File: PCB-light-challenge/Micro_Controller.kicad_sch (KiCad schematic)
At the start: 11 parts, among them J1 Conn_01x16_Socket, J3 Conn_01x13_Socket

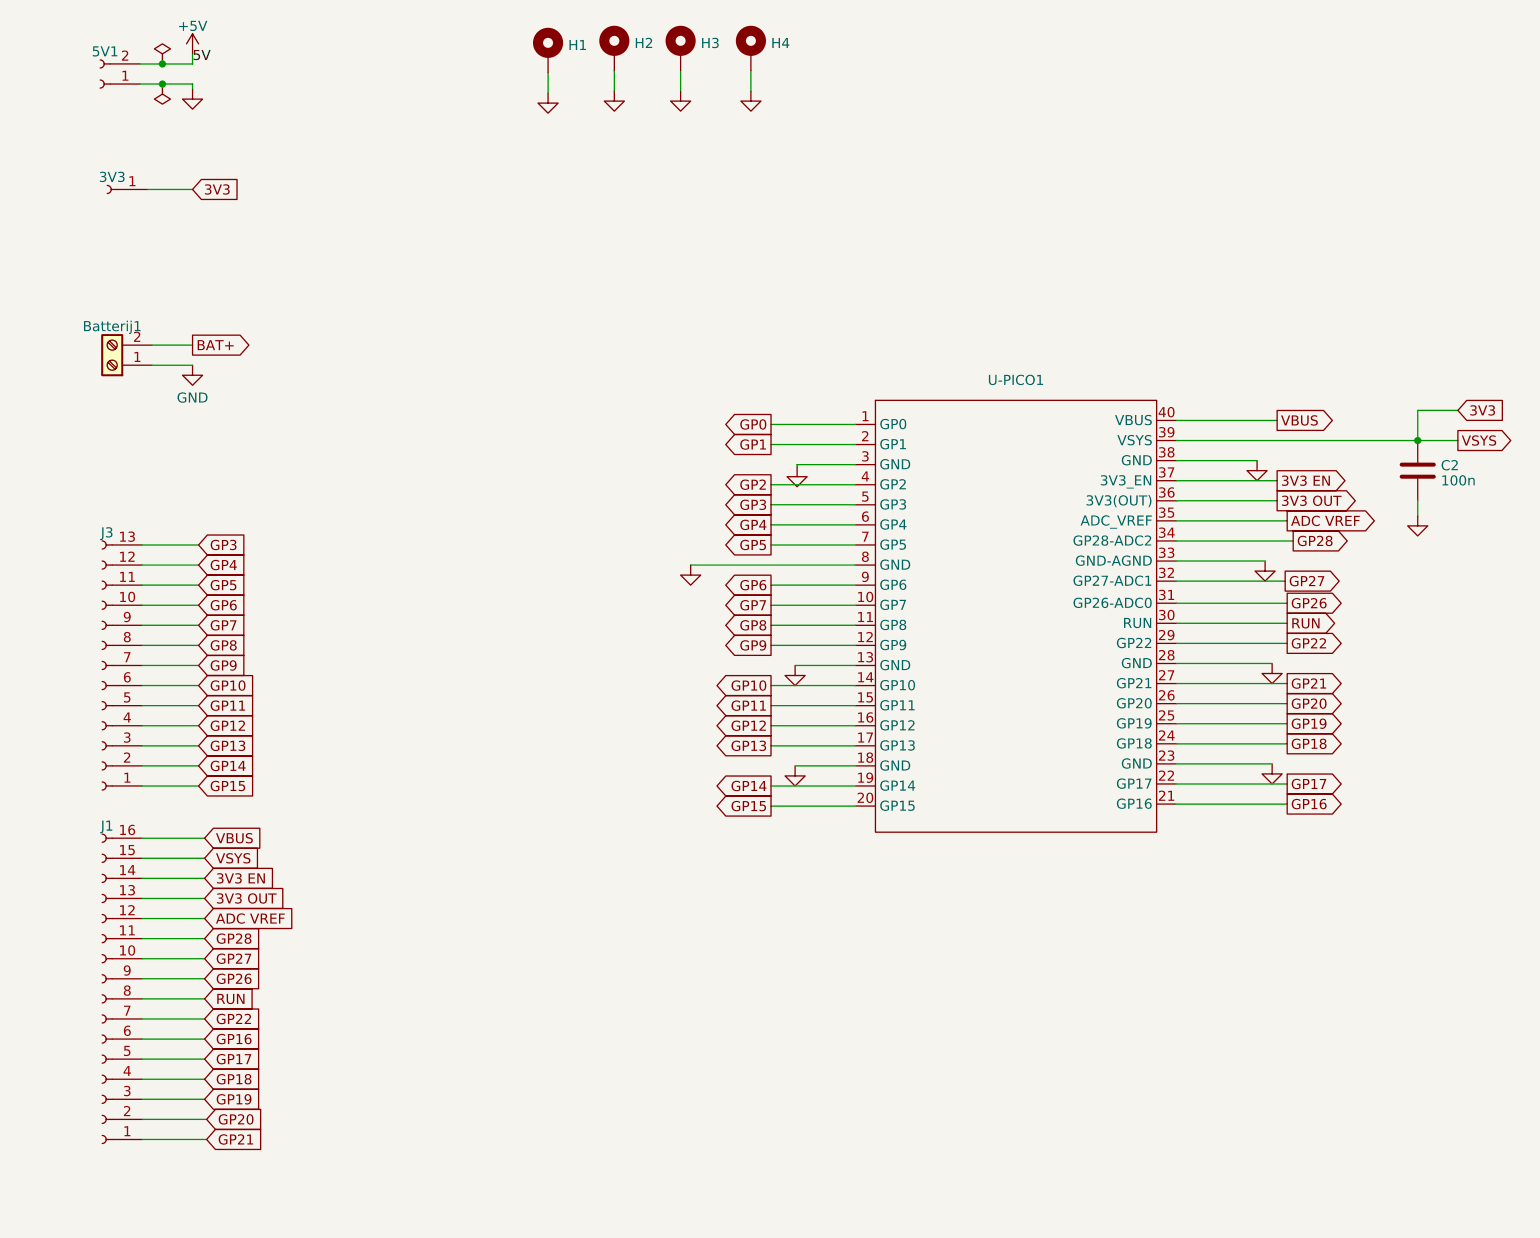
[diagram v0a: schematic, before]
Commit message: TP footprint verandert,  apparte grond (P-) gemaakt.  AC  clearance verandert.  connector voor PIR verandert
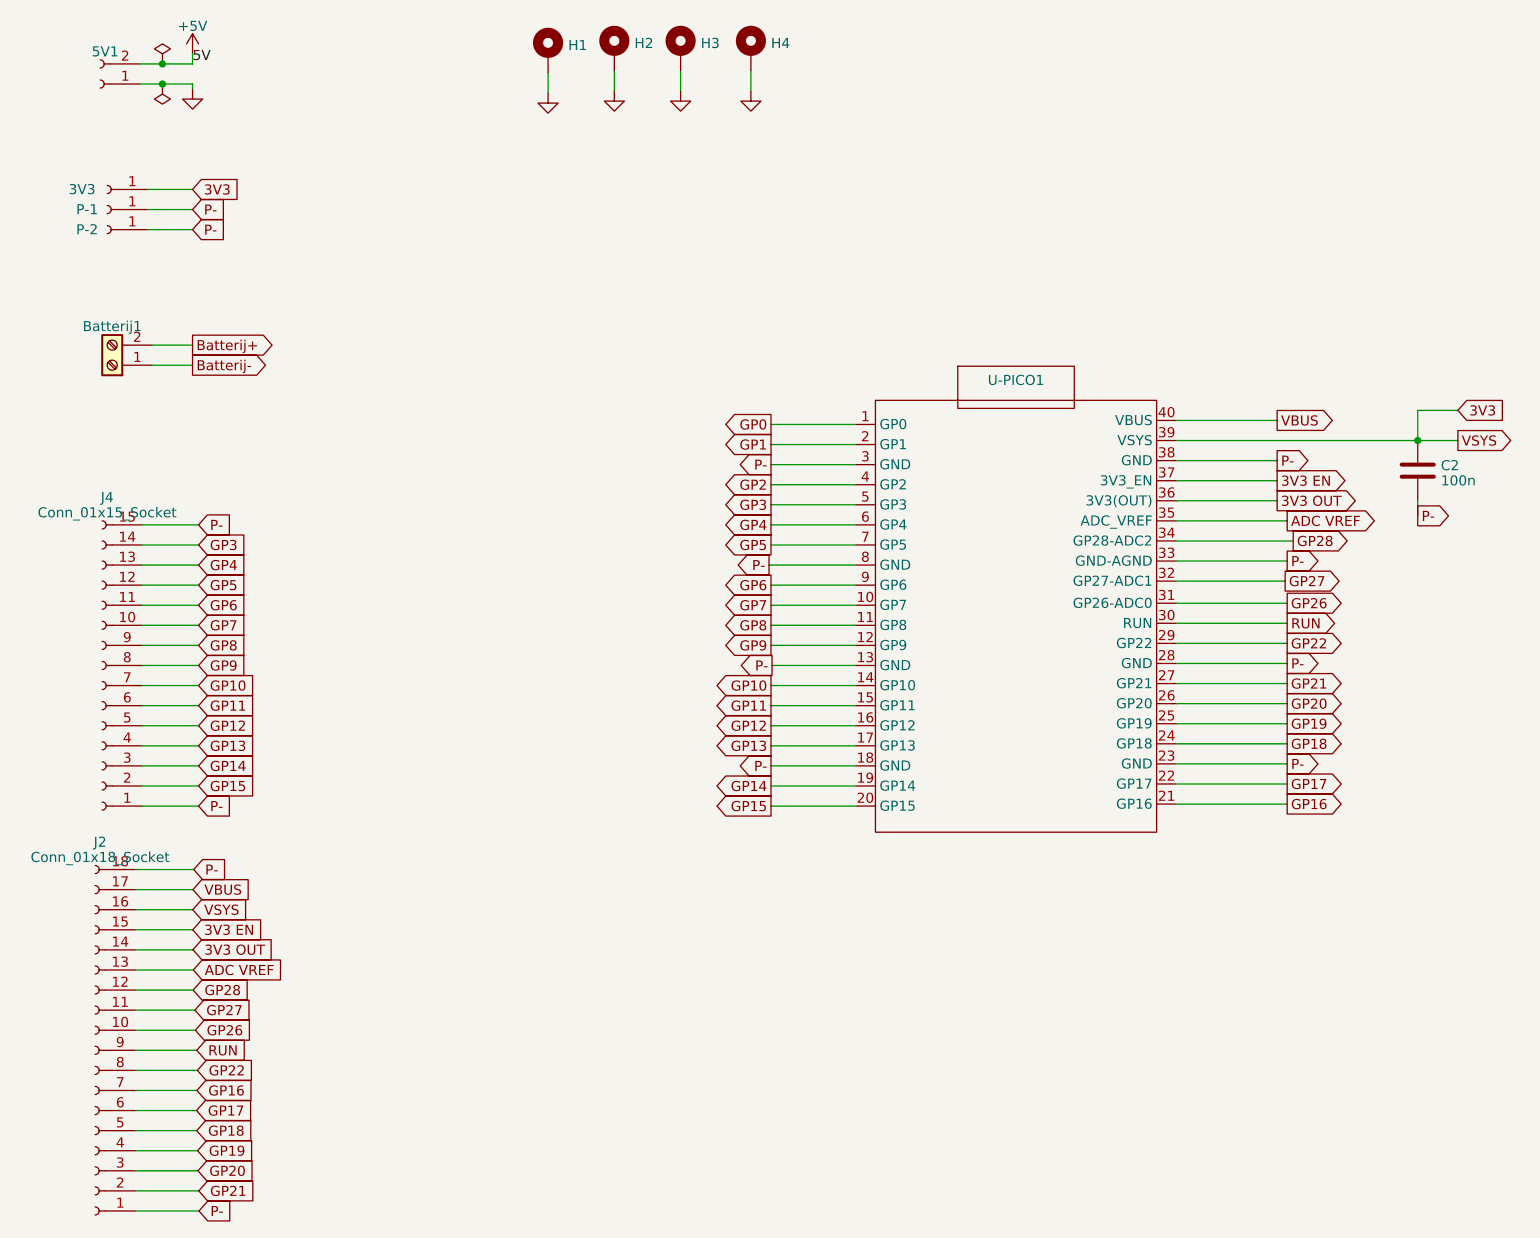
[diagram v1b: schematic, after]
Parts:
- removed J1: Conn_01x16_Socket, Connector_PinHeader_2.54mm:PinHeader_1x16_P2.54mm_Vertical, symbol Connector:Conn_01x16_Socket
- removed J3: Conn_01x13_Socket, Connector_PinHeader_2.54mm:PinHeader_1x13_P2.54mm_Vertical, symbol Connector:Conn_01x13_Socket
- added J2: Conn_01x18_Socket, Connector_PinSocket_2.54mm:PinSocket_1x18_P2.54mm_Vertical, symbol Connector:Conn_01x18_Socket
- added J4: Conn_01x15_Socket, Connector_PinSocket_2.54mm:PinSocket_1x15_P2.54mm_Vertical, symbol Connector:Conn_01x15_Socket
- added P-1, P-2: Conn_01x01_Socket, Connector_PinHeader_2.54mm:PinHeader_1x01_P2.54mm_Vertical, symbol Connector:Conn_01x01_Socket
- 5V1: footprint Connector_PinHeader_2.54mm:PinHeader_1x02_P2.54mm_Vertical -> TerminalBlock_TE-Connectivity:TerminalBlock_TE_282834-2_1x02_P2.54mm_Horizontal
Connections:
- net 3V3: now also J2.16 (Pin_16)
- net 3V3 EN: now also J2.15 (Pin_15)
- net 3V3 OUT: now also J2.14 (Pin_14)
- net ADC VREF: now also J2.13 (Pin_13)
- net GND: no longer Batterij1.1 (Pin_1), C2.2, U-PICO1.13 (GND), U-PICO1.18 (GND), U-PICO1.23 (GND), U-PICO1.28 (GND), U-PICO1.3 (GND), U-PICO1.33 (GND-AGND), U-PICO1.38 (GND), U-PICO1.8 (GND)
- net GP10: now also J4.7 (Pin_7)
- net GP11: now also J4.6 (Pin_6)
- net GP12: now also J4.5 (Pin_5)
- net GP13: now also J4.4 (Pin_4)
- net GP14: now also J4.3 (Pin_3)
- net GP15: now also J4.2 (Pin_2)
- net GP16: now also J2.7 (Pin_7)
- net GP17: now also J2.6 (Pin_6)
- net GP18: now also J2.5 (Pin_5)
- net GP19: now also J2.4 (Pin_4)
- net GP20: now also J2.3 (Pin_3)
- net GP21: now also J2.2 (Pin_2)
- net GP22: now also J2.8 (Pin_8)
- net GP26: now also J2.10 (Pin_10)
- net GP27: now also J2.11 (Pin_11)
- net GP28: now also J2.12 (Pin_12)
- net GP3: now also J4.14 (Pin_14)
- net GP4: now also J4.13 (Pin_13)
- net GP5: now also J4.12 (Pin_12)
- net GP6: now also J4.11 (Pin_11)
- net GP7: now also J4.10 (Pin_10)
- net GP8: now also J4.9 (Pin_9)
- net GP9: now also J4.8 (Pin_8)
- net RUN: now also J2.9 (Pin_9)
- net VBUS: now also J2.17 (Pin_17)
- net BAT+ renamed Batterij+
- new net Batterij-: Batterij1.1 (Pin_1)
- new net P-: C2.2, J2.1 (Pin_1), J2.18 (Pin_18), J4.1 (Pin_1), J4.15 (Pin_15), P-1.1 (Pin_1), P-2.1 (Pin_1), U-PICO1.13 (GND), U-PICO1.18 (GND), U-PICO1.23 (GND), U-PICO1.28 (GND), U-PICO1.3 (GND), U-PICO1.33 (GND-AGND), U-PICO1.38 (GND), U-PICO1.8 (GND)

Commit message: Vias  kleiner gemaakt en grond GND genoemd op silkscreen
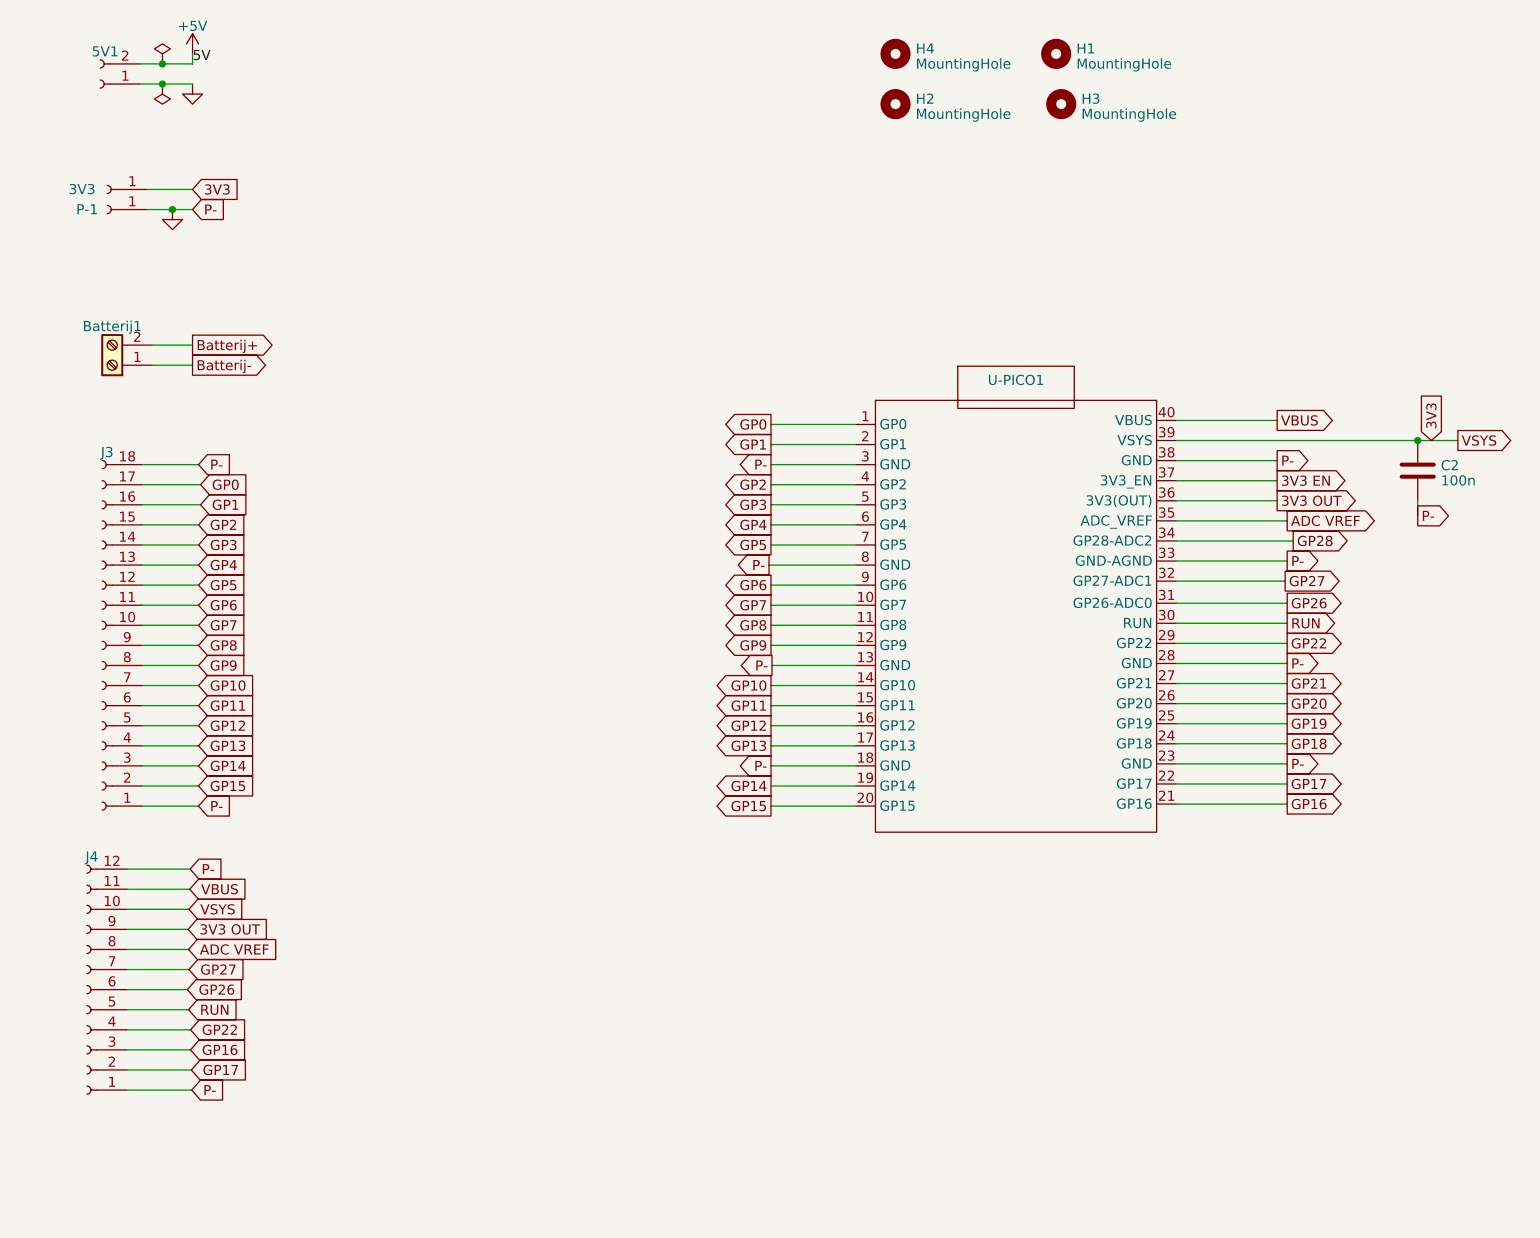
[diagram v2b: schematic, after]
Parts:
- removed H1, H2, H3, H4: MountingHole_Pad, MountingHole:MountingHole_2.2mm_M2_DIN965_Pad, symbol Mechanical:MountingHole_Pad
- removed J2: Conn_01x18_Socket, Connector_PinSocket_2.54mm:PinSocket_1x18_P2.54mm_Vertical, symbol Connector:Conn_01x18_Socket
- removed J4: Conn_01x15_Socket, Connector_PinSocket_2.54mm:PinSocket_1x15_P2.54mm_Vertical, symbol Connector:Conn_01x15_Socket
- removed P-2: Conn_01x01_Socket, Connector_PinHeader_2.54mm:PinHeader_1x01_P2.54mm_Vertical, symbol Connector:Conn_01x01_Socket
- added H1, H2, H3, H4: MountingHole, MountingHole:MountingHole_2.2mm_M2_DIN965_Pad, symbol Mechanical:MountingHole
- added J3: Conn_01x18_Socket, Connector_PinSocket_2.54mm:PinSocket_1x18_P2.54mm_Vertical, symbol Connector:Conn_01x18_Socket
- added J4: Conn_01x12_Socket, Connector_PinSocket_2.54mm:PinSocket_1x12_P2.54mm_Vertical, symbol Connector:Conn_01x12_Socket
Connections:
- net P- is gone; now on net GND: C2.2, P-1.1 (Pin_1), U-PICO1.13 (GND), U-PICO1.18 (GND), U-PICO1.23 (GND), U-PICO1.28 (GND), U-PICO1.3 (GND), U-PICO1.33 (GND-AGND), U-PICO1.38 (GND), U-PICO1.8 (GND)
- net 3V3: now also J4.10 (Pin_10)
- net 3V3 OUT: now also J4.9 (Pin_9)
- net ADC VREF: now also J4.8 (Pin_8)
- net GND: now also J3.1 (Pin_1), J3.18 (Pin_18), J4.1 (Pin_1), J4.12 (Pin_12)
- net GP0: now also J3.17 (Pin_17)
- net GP1: now also J3.16 (Pin_16)
- net GP10: now also J3.7 (Pin_7)
- net GP11: now also J3.6 (Pin_6)
- net GP12: now also J3.5 (Pin_5)
- net GP13: now also J3.4 (Pin_4)
- net GP14: now also J3.3 (Pin_3)
- net GP15: now also J3.2 (Pin_2)
- net GP16: now also J4.3 (Pin_3)
- net GP17: now also J4.2 (Pin_2)
- net GP2: now also J3.15 (Pin_15)
- net GP22: now also J4.4 (Pin_4)
- net GP26: now also J4.6 (Pin_6)
- net GP27: now also J4.7 (Pin_7)
- net GP3: now also J3.14 (Pin_14)
- net GP4: now also J3.13 (Pin_13)
- net GP5: now also J3.12 (Pin_12)
- net GP6: now also J3.11 (Pin_11)
- net GP7: now also J3.10 (Pin_10)
- net GP8: now also J3.9 (Pin_9)
- net GP9: now also J3.8 (Pin_8)
- net RUN: now also J4.5 (Pin_5)
- net VBUS: now also J4.11 (Pin_11)

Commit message: LDR connector, silkscreen AC,  Mounting hole main pcb aangepast
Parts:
- H1, H2, H3, H4: footprint MountingHole:MountingHole_2.2mm_M2_DIN965_Pad -> MountingHole:MountingHole_3.2mm_M3_DIN965_Pad
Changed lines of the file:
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@@
       (effects (font (size 1.27 1.27)) (justify left))
     )
-    (property "Footprint" "MountingHole:MountingHole_2.2mm_M2_DIN965_Pad" (at 149.225 36.195 0)
+    (property "Footprint" "MountingHole:MountingHole_3.2mm_M3_DIN965_Pad" (at 149.225 36.195 0)
       (effects (font (size 1.27 1.27)) hide)
     )
@@
       (effects (font (size 1.27 1.27)) (justify left))
     )
-    (property "Footprint" "MountingHole:MountingHole_2.2mm_M2_DIN965_Pad" (at 128.27 29.845 0)
+    (property "Footprint" "MountingHole:MountingHole_3.2mm_M3_DIN965_Pad" (at 128.27 29.845 0)
       (effects (font (size 1.27 1.27)) hide)
     )
@@
       (effects (font (size 1.27 1.27)) (justify left))
     )
-    (property "Footprint" "MountingHole:MountingHole_2.2mm_M2_DIN965_Pad" (at 128.27 36.195 0)
+    (property "Footprint" "MountingHole:MountingHole_3.2mm_M3_DIN965_Pad" (at 128.27 36.195 0)
       (effects (font (size 1.27 1.27)) hide)
     )
@@
       (effects (font (size 1.27 1.27)) (justify left))
     )
-    (property "Footprint" "MountingHole:MountingHole_2.2mm_M2_DIN965_Pad" (at 148.59 29.845 0)
-      (effects (font (size 1.27 1.27)) hide)
-    )
+    (property "Footprint" "MountingHole:MountingHole_3.2mm_M3_DIN965_Pad" (at 148.59 29.845 0)
+      (effects (font (size 1.27 1.27)) hide)
+    )
